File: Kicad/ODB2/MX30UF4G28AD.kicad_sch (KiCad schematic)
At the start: 0 parts

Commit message: edit titles
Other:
- company: (none) -> GAUL
- title: (none) -> NAND Memory
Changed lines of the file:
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@@
 	(generator_version "8.0")
 	(paper "A4")
+	(title_block
+		(title "NAND Memory")
+		(date "2024-11-09")
+		(company "GAUL")
+	)
 )

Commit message: add titles
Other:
- note added: "NAND Memery"
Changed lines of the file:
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@@
 		(company "GAUL")
 	)
+	(text "NAND Memery"
+		(exclude_from_sim no)
+		(at 44.196 18.542 0)
+		(effects
+			(font
+				(size 6 6)
+				(thickness 1.2)
+				(bold yes)
+			)
+		)
+	)
 )

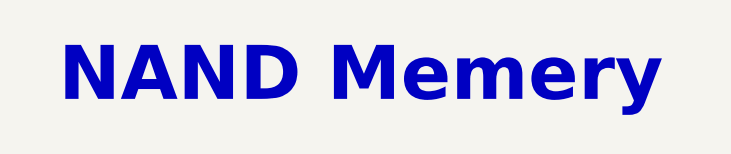
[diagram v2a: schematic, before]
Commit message: Memery-->Memory
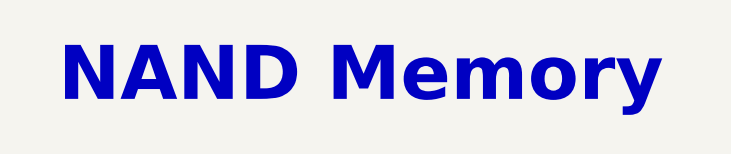
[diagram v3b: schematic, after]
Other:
- note added: "NAND Memory"
- note removed: "NAND Memery"
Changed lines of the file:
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@@
 		(company "GAUL")
 	)
-	(text "NAND Memery"
+	(text "NAND Memory"
 		(exclude_from_sim no)
 		(at 44.196 18.542 0)

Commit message: add Buzzer
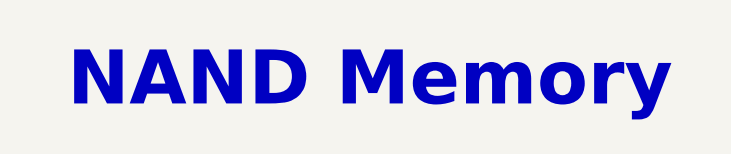
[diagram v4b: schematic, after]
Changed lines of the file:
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@@
 	(text "NAND Memory"
 		(exclude_from_sim no)
-		(at 44.196 18.542 0)
+		(at 45.212 19.05 0)
 		(effects
 			(font
